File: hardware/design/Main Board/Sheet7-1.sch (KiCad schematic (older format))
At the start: 36 parts

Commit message: Version 1.0
Wrapped up design. Version for Detailed Design Review.
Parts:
- removed Q? (x8): BSS138, SOT-23, symbol BSS138
- removed R? (x16): 10K, ~, symbol R
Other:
- moved on the sheet: Q?, R?

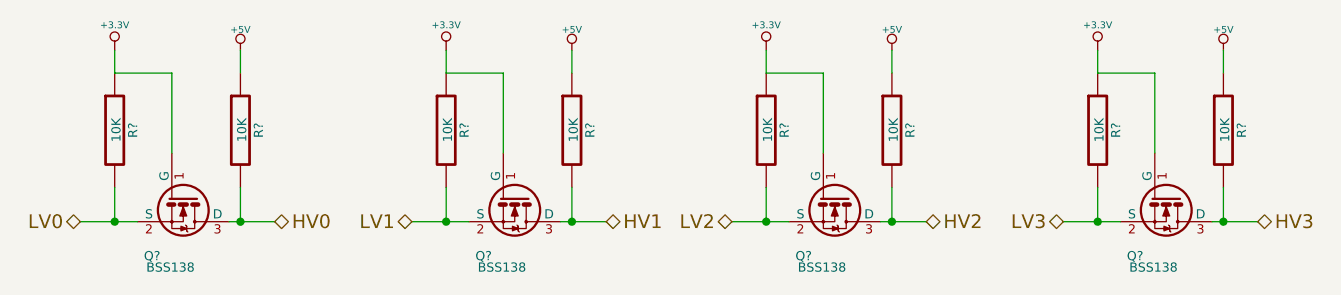
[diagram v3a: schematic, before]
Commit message: Version 1.0.082514.2134
Initial partial PCB layout.
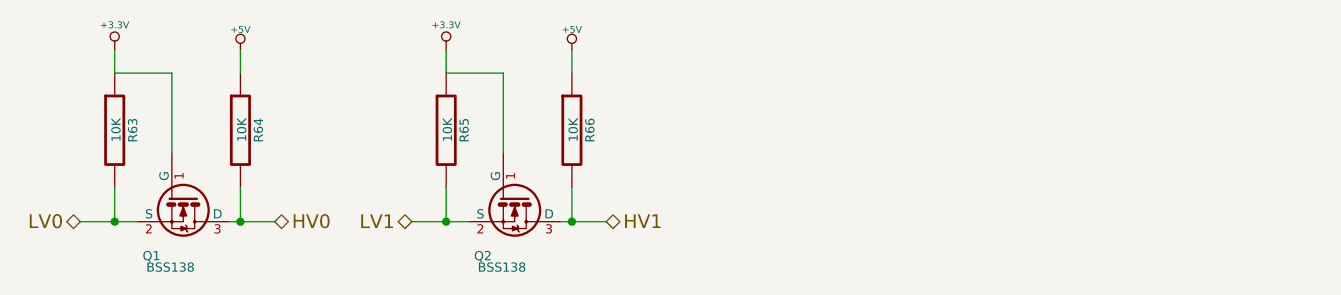
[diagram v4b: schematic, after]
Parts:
- removed Q? (x2): BSS138, SOT-23, symbol BSS138
- removed R? (x4): 10K, ~, symbol R
- gave numbers to parts that had none: 6
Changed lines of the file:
@@
 Sheet 8 9
 Title "Hybrid Audio Dynamics Processor"
-Date "15 may 2014"
+Date "26 aug 2014"
 Rev "1.0"
 Comp "P14345"
@@
 $EndDescr
 $Comp
-L BSS138 Q?
+L BSS138 Q1
 U 1 1 53681F7F
 P 3600 4600
-F 0 "Q?" V 3850 4500 40  0000 R CNN
+F 0 "Q1" V 3850 4500 40  0000 R CNN
 F 1 "BSS138" V 3900 4650 40  0000 R CNN
 F 2 "SOT-23" V 3950 4500 29  0001 C CNN
@@
 $EndComp
 $Comp
-L R R?
+L R R63
 U 1 1 53681FCC
 P 3300 4300
-F 0 "R?" V 3380 4300 40  0000 C CNN
+F 0 "R63" V 3380 4300 40  0000 C CNN
 F 1 "10K" V 3307 4301 40  0000 C CNN
 F 2 "~" V 3230 4300 30  0000 C CNN
@@
 $EndComp
 $Comp
-L R R?
+L R R64
 U 1 1 53681FD9
 P 3850 4300
-F 0 "R?" V 3930 4300 40  0000 C CNN
+F 0 "R64" V 3930 4300 40  0000 C CNN
 F 1 "10K" V 3857 4301 40  0000 C CNN
 F 2 "~" V 3780 4300 30  0000 C CNN
@@
 	3850 4050 3850 3950
 $Comp
-L +3.3V #PWR?
+L +3.3V #PWR0113
 U 1 1 53682005
 P 3300 3950
-F 0 "#PWR?" H 3300 3910 30  0001 C CNN
+F 0 "#PWR0113" H 3300 3910 30  0001 C CNN
 F 1 "+3.3V" H 3300 4060 30  0000 C CNN
 F 2 "" H 3300 3950 60  0000 C CNN
@@
 $EndComp
 $Comp
-L +5V #PWR?
+L +5V #PWR0114
 U 1 1 53682014
 P 3850 3950
-F 0 "#PWR?" H 3850 4040 20  0001 C CNN
+F 0 "#PWR0114" H 3850 4040 20  0001 C CNN
 F 1 "+5V" H 3850 4040 30  0000 C CNN
 F 2 "" H 3850 3950 60  0000 C CNN
@@
 HV0
 $Comp
-L BSS138 Q?
+L BSS138 Q2
 U 1 1 53682038
 P 5050 4600
-F 0 "Q?" V 5300 4500 40  0000 R CNN
+F 0 "Q2" V 5300 4500 40  0000 R CNN
 F 1 "BSS138" V 5350 4650 40  0000 R CNN
 F 2 "SOT-23" V 5400 4500 29  0001 C CNN
@@
 $EndComp
 $Comp
-L R R?
+L R R65
 U 1 1 5368203E
 P 4750 4300
-F 0 "R?" V 4830 4300 40  0000 C CNN
+F 0 "R65" V 4830 4300 40  0000 C CNN
 F 1 "10K" V 4757 4301 40  0000 C CNN
 F 2 "~" V 4680 4300 30  0000 C CNN
@@
 $EndComp
 $Comp
-L R R?
+L R R66
 U 1 1 53682044
 P 5300 4300
-F 0 "R?" V 5380 4300 40  0000 C CNN
+F 0 "R66" V 5380 4300 40  0000 C CNN
 F 1 "10K" V 5307 4301 40  0000 C CNN
 F 2 "~" V 5230 4300 30  0000 C CNN
@@
 	5300 4050 5300 3950
 $Comp
-L +3.3V #PWR?
+L +3.3V #PWR0115
 U 1 1 53682052
 P 4750 3950
-F 0 "#PWR?" H 4750 3910 30  0001 C CNN
+F 0 "#PWR0115" H 4750 3910 30  0001 C CNN
 F 1 "+3.3V" H 4750 4060 30  0000 C CNN
 F 2 "" H 4750 3950 60  0000 C CNN
@@
 $EndComp
 $Comp
-L +5V #PWR?
+L +5V #PWR0116
 U 1 1 53682058
 P 5300 3950
-F 0 "#PWR?" H 5300 4040 20  0001 C CNN
+F 0 "#PWR0116" H 5300 4040 20  0001 C CNN
 F 1 "+5V" H 5300 4040 30  0000 C CNN
 F 2 "" H 5300 3950 60  0000 C CNN
@@
 Text HLabel 5450 4700 2    60   BiDi ~ 0
 HV1
-$Comp
-L BSS138 Q?
-U 1 1 53682087
-P 6450 4600
-F 0 "Q?" V 6700 4500 40  0000 R CNN
-F 1 "BSS138" V 6750 4650 40  0000 R CNN
-F 2 "SOT-23" V 6800 4500 29  0001 C CNN
-F 3 "~" H 6450 4600 60  0000 C CNN
-	1    6450 4600
-	0    1    1    0
-$EndComp
-$Comp
-L R R?
-U 1 1 5368208D
-P 6150 4300
-F 0 "R?" V 6230 4300 40  0000 C CNN
-F 1 "10K" V 6157 4301 40  0000 C CNN
-F 2 "~" V 6080 4300 30  0000 C CNN
-F 3 "~" H 6150 4300 30  0000 C CNN
-	1    6150 4300
-	1    0    0    -1
-$EndComp
-$Comp
-L R R?
-U 1 1 53682093
-P 6700 4300
-F 0 "R?" V 6780 4300 40  0000 C CNN
-F 1 "10K" V 6707 4301 40  0000 C CNN
-F 2 "~" V 6630 4300 30  0000 C CNN
-F 3 "~" H 6700 4300 30  0000 C CNN
-	1    6700 4300
-	1    0    0    -1
-$EndComp
-Wire Wire Line
-	6150 4050 6400 4050
-Wire Wire Line
-	6400 4050 6400 4400
-Wire Wire Line
-	6150 4550 6150 4700
-Wire Wire Line
-	6000 4700 6250 4700
-Wire Wire Line
-	6650 4700 6850 4700
-Wire Wire Line
-	6700 4700 6700 4550
-Wire Wire Line
-	6150 4050 6150 3950
-Wire Wire Line
-	6700 4050 6700 3950
-$Comp
-L +3.3V #PWR?
-U 1 1 536820A1
-P 6150 3950
-F 0 "#PWR?" H 6150 3910 30  0001 C CNN
-F 1 "+3.3V" H 6150 4060 30  0000 C CNN
-F 2 "" H 6150 3950 60  0000 C CNN
-F 3 "" H 6150 3950 60  0000 C CNN
-	1    6150 3950
-	1    0    0    -1
-$EndComp
-$Comp
-L +5V #PWR?
-U 1 1 536820A7
-P 6700 3950
-F 0 "#PWR?" H 6700 4040 20  0001 C CNN
-F 1 "+5V" H 6700 4040 30  0000 C CNN
-F 2 "" H 6700 3950 60  0000 C CNN
-F 3 "" H 6700 3950 60  0000 C CNN
-	1    6700 3950
-	1    0    0    -1
-$EndComp
-Connection ~ 6150 4700
-Connection ~ 6700 4700
-Text HLabel 6000 4700 0    60   BiDi ~ 0
-LV2
-Text HLabel 6850 4700 2    60   BiDi ~ 0
-HV2
-$Comp
-L BSS138 Q?
-U 1 1 536820B1
-P 7900 4600
-F 0 "Q?" V 8150 4500 40  0000 R CNN
-F 1 "BSS138" V 8200 4650 40  0000 R CNN
-F 2 "SOT-23" V 8250 4500 29  0001 C CNN
-F 3 "~" H 7900 4600 60  0000 C CNN
-	1    7900 4600
-	0    1    1    0
-$EndComp
-$Comp
-L R R?
-U 1 1 536820B7
-P 7600 4300
-F 0 "R?" V 7680 4300 40  0000 C CNN
-F 1 "10K" V 7607 4301 40  0000 C CNN
-F 2 "~" V 7530 4300 30  0000 C CNN
-F 3 "~" H 7600 4300 30  0000 C CNN
-	1    7600 4300
-	1    0    0    -1
-$EndComp
-$Comp
-L R R?
-U 1 1 536820BD
-P 8150 4300
-F 0 "R?" V 8230 4300 40  0000 C CNN
-F 1 "10K" V 8157 4301 40  0000 C CNN
-F 2 "~" V 8080 4300 30  0000 C CNN
-F 3 "~" H 8150 4300 30  0000 C CNN
-	1    8150 4300
-	1    0    0    -1
-$EndComp
-Wire Wire Line
-	7600 4050 7850 4050
-Wire Wire Line
-	7850 4050 7850 4400
-Wire Wire Line
-	7600 4550 7600 4700
-Wire Wire Line
-	7450 4700 7700 4700
-Wire Wire Line
-	8100 4700 8300 4700
-Wire Wire Line
-	8150 4700 8150 4550
-Wire Wire Line
-	7600 4050 7600 3950
-Wire Wire Line
-	8150 4050 8150 3950
-$Comp
-L +3.3V #PWR?
-U 1 1 536820CB
-P 7600 3950
-F 0 "#PWR?" H 7600 3910 30  0001 C CNN
-F 1 "+3.3V" H 7600 4060 30  0000 C CNN
-F 2 "" H 7600 3950 60  0000 C CNN
-F 3 "" H 7600 3950 60  0000 C CNN
-	1    7600 3950
-	1    0    0    -1
-$EndComp
-$Comp
-L +5V #PWR?
-U 1 1 536820D1
-P 8150 3950
-F 0 "#PWR?" H 8150 4040 20  0001 C CNN
-F 1 "+5V" H 8150 4040 30  0000 C CNN
-F 2 "" H 8150 3950 60  0000 C CNN
-F 3 "" H 8150 3950 60  0000 C CNN
-	1    8150 3950
-	1    0    0    -1
-$EndComp
-Connection ~ 7600 4700
-Connection ~ 8150 4700
-Text HLabel 7450 4700 0    60   BiDi ~ 0
-LV3
-Text HLabel 8300 4700 2    60   BiDi ~ 0
-HV3
 $EndSCHEMATC
